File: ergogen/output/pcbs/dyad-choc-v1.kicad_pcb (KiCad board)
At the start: 2 copper layers, 117.6 x 96.6 mm, 84 parts

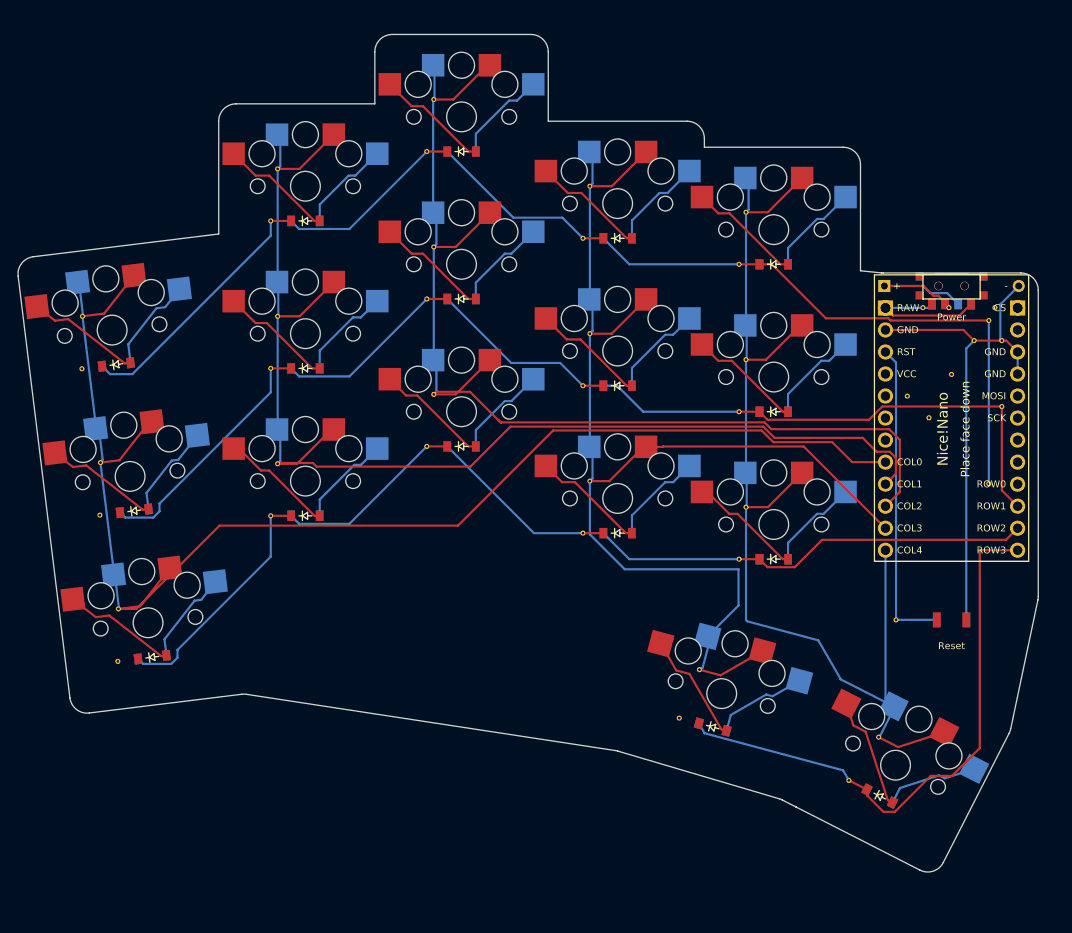
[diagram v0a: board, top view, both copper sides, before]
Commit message: Rename and adding reverse side labels
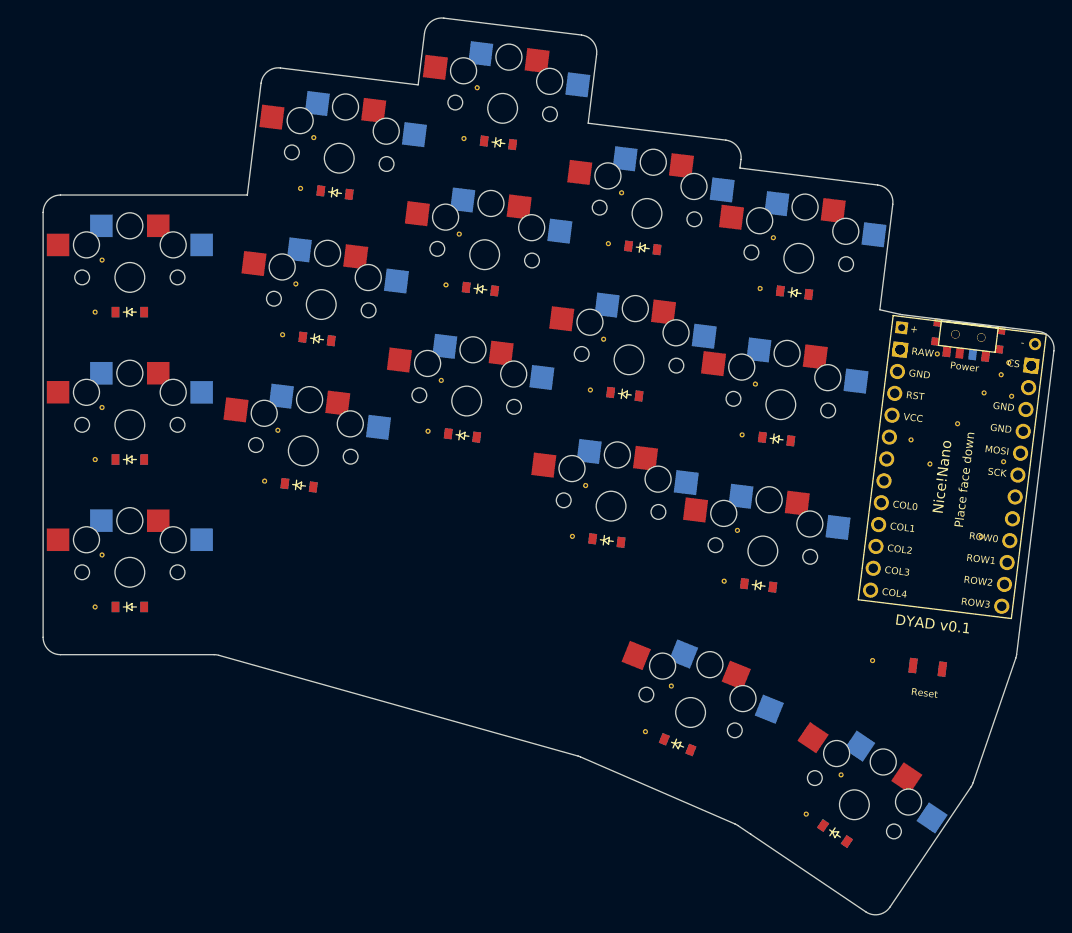
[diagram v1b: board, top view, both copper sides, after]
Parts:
- removed the REF** at (257.3, 133.3)
- removed the REF** at (156.5, 153.4)
- removed the REF** at (231.0, 135.5)
- removed the REF** at (259.0, 149.8)
- removed the REF** at (230.2, 124.5)
- removed the REF** at (177.0, 130.5)
- removed the REF** at (158.6, 170.3)
- removed the REF** at (176.2, 119.5)
- removed the REF** at (251.4, 129.5)
- removed the REF** at (213.0, 132.5)
- removed the REF** at (194.2, 145.5)
- removed the REF** at (225.7, 171.2)
- removed the REF** at (194.2, 111.5)
- removed the REF** at (176.2, 136.5)
- removed the REF** at (231.0, 152.5)
- removed the REF** at (195.0, 139.5)
- removed the REF** at (231.0, 118.5)
- removed the REF** at (212.2, 155.5)
- removed the REF** at (254.7, 137.2)
- removed the REF** at (254.4, 129.5)
- removed the REF** at (177.0, 113.5)
- removed the REF** at (223.3, 176.8)
- removed the REF** at (248.3, 165.5)
- removed the REF** at (176.2, 153.5)
- removed the REF** at (154.5, 136.5)
- removed the REF** at (246.3, 179.0)
- removed the REF** at (212.2, 121.5)
- removed the REF** at (154.5, 130.5)
- removed the REF** at (213.0, 149.5)
- removed the REF** at (252.1, 142.2)
- removed the REF** at (195.0, 105.5)
- removed the REF** at (260.5, 140.9)
- removed the REF** at (230.2, 141.5)
- removed the REF** at (259.7, 129.5)
- removed the REF** at (194.2, 128.5)
- removed the REF** at (158.7, 164.2)
- removed the REF** at (195.0, 122.5)
- removed the REF** at (260.5, 133.3)
- removed the REF** at (230.2, 158.5)
- removed the REF** at (249.6, 139.7)
- removed the REF** at (213.0, 115.5)
- removed the REF** at (242.9, 184.0)
- removed the REF** at (156.6, 147.4)
- removed the REF** at (259.0, 131.0)
- removed the REF** at (177.0, 147.5)
- removed the REF** at (212.2, 138.5)
- added REF**: VIA-0.6mm, VIA-0.6mm, F.Cu at (156.0, 164.0)
- added REF**: VIA-0.6mm, VIA-0.6mm, F.Cu at (211.0, 155.9)
- added REF**: VIA-0.6mm, VIA-0.6mm, F.Cu at (213.1, 139.0)
- added REF**: VIA-0.6mm, VIA-0.6mm, F.Cu at (215.2, 122.1)
- added REF**: VIA-0.6mm, VIA-0.6mm, F.Cu at (228.5, 161.0)
- added REF**: VIA-0.6mm, VIA-0.6mm, F.Cu at (230.6, 144.2)
- added REF**: VIA-0.6mm, VIA-0.6mm, F.Cu at (232.7, 127.3)
- added REF**: VIA-0.6mm, VIA-0.6mm, F.Cu at (219.4, 178.4)
- added REF**: VIA-0.6mm, VIA-0.6mm, F.Cu at (238.0, 187.9)
- added REF**: VIA-0.6mm, VIA-0.6mm, F.Cu at (156.8, 158.0)
- added REF**: VIA-0.6mm, VIA-0.6mm, F.Cu at (156.8, 141.0)
- added REF**: VIA-0.6mm, VIA-0.6mm, F.Cu at (156.0, 147.0)
- added REF**: VIA-0.6mm, VIA-0.6mm, F.Cu at (156.8, 124.0)
- added REF**: VIA-0.6mm, VIA-0.6mm, F.Cu at (177.1, 143.6)
- added REF**: VIA-0.6mm, VIA-0.6mm, F.Cu at (179.1, 126.8)
- added REF**: VIA-0.6mm, VIA-0.6mm, F.Cu at (181.2, 109.9)
- added REF**: VIA-0.6mm, VIA-0.6mm, F.Cu at (195.9, 137.9)
- added REF**: VIA-0.6mm, VIA-0.6mm, F.Cu at (198.0, 121.0)
- added REF**: VIA-0.6mm, VIA-0.6mm, F.Cu at (200.1, 104.1)
- added REF**: VIA-0.6mm, VIA-0.6mm, F.Cu at (212.6, 150.0)
- added REF**: VIA-0.6mm, VIA-0.6mm, F.Cu at (214.6, 133.1)
- added REF**: VIA-0.6mm, VIA-0.6mm, F.Cu at (216.7, 116.3)
- added REF**: VIA-0.6mm, VIA-0.6mm, F.Cu at (156.0, 130.0)
- added REF**: VIA-0.6mm, VIA-0.6mm, F.Cu at (230.1, 155.2)
- added REF**: VIA-0.6mm, VIA-0.6mm, F.Cu at (232.1, 138.3)
- added REF**: VIA-0.6mm, VIA-0.6mm, F.Cu at (234.2, 121.4)
- added REF**: VIA-0.6mm, VIA-0.6mm, F.Cu at (222.4, 173.1)
- added REF**: VIA-0.6mm, VIA-0.6mm, F.Cu at (242.0, 183.4)
- added REF**: VIA-0.6mm, VIA-0.6mm, F.Cu at (261.7, 139.7)
- added REF**: VIA-0.6mm, VIA-0.6mm, F.Cu at (258.5, 139.3)
- added REF**: VIA-0.6mm, VIA-0.6mm, F.Cu at (260.5, 137.2)
- added REF**: VIA-0.6mm, VIA-0.6mm, F.Cu at (258.2, 155.9)
- added REF**: VIA-0.6mm, VIA-0.6mm, F.Cu at (261.3, 135.8)
- added REF**: VIA-0.6mm, VIA-0.6mm, F.Cu at (175.5, 149.5)
- added REF**: VIA-0.6mm, VIA-0.6mm, F.Cu at (250.1, 144.7)
- added REF**: VIA-0.6mm, VIA-0.6mm, F.Cu at (252.3, 147.5)
- added REF**: VIA-0.6mm, VIA-0.6mm, F.Cu at (253.1, 134.8)
- added REF**: VIA-0.6mm, VIA-0.6mm, F.Cu at (255.4, 142.9)
- added REF**: VIA-0.6mm, VIA-0.6mm, F.Cu at (260.7, 147.3)
- added REF**: VIA-0.6mm, VIA-0.6mm, F.Cu at (245.6, 170.2)
- added REF**: VIA-0.6mm, VIA-0.6mm, F.Cu at (177.6, 132.6)
- added REF**: VIA-0.6mm, VIA-0.6mm, F.Cu at (179.7, 115.7)
- added REF**: VIA-0.6mm, VIA-0.6mm, F.Cu at (194.4, 143.7)
- added REF**: VIA-0.6mm, VIA-0.6mm, F.Cu at (196.5, 126.9)
- added REF**: VIA-0.6mm, VIA-0.6mm, F.Cu at (198.5, 110.0)
- moved D17 6.73 mm to (241.3, 190.1), turned to -34 degrees
- moved S17 6.58 mm to (243.5, 186.8), turned to -34 degrees
- moved S3 6.41 mm to (160.0, 126.0), turned to 0 degrees
- moved D1 6.34 mm to (160.0, 164.0), turned to 0 degrees
- moved D3 6.24 mm to (160.0, 130.0), turned to 0 degrees
- moved S1 6.19 mm to (160.0, 160.0), turned to 0 degrees
- moved ? 6.13 mm to (252.0, 171.0), turned to 173 degrees
- moved ? 6.08 mm to (256.7, 132.7), turned to -97 degrees
- moved T1 6.08 mm to (256.7, 132.7), turned to -7 degrees
- moved S2 5.95 mm to (160.0, 143.0), turned to 0 degrees
- moved D2 5.94 mm to (160.0, 147.0), turned to 0 degrees
- moved MCU1 5.64 mm to (254.7, 149.1), turned to -97 degrees
- moved S6 5.06 mm to (184.1, 112.3), turned to -7 degrees
- moved S9 4.84 mm to (203.0, 106.5), turned to -7 degrees
- moved D6 4.72 mm to (183.7, 116.2), turned to -7 degrees
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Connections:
- MCU1 pad : RAW -> CS
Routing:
- net COL0: track 161.3 -> 0.00 mm
- net ROW0: track 141.9 -> 0.00 mm
- net COL1: track 141.4 -> 0.00 mm
- net COL3: track 141.2 -> 0.00 mm
- net ROW1: track 133.9 -> 0.00 mm
- net COL2: track 128.0 -> 0.00 mm
- net COL4: track 127.1 -> 0.00 mm
- net ROW2: track 123.7 -> 0.00 mm
- net ROW3: track 66.2 -> 0.00 mm
- net GND: track 58.7 -> 0.00 mm
- net RST: track 36.1 -> 0.00 mm
- net pinky_top: track 24.2 -> 0.00 mm
- net ring_home: track 24.2 -> 0.00 mm
- net middle_top: track 24.2 -> 0.00 mm
- net inner_home: track 24.2 -> 0.00 mm
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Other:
- board size 117.6 x 96.6 mm -> 116.6 x 103.4 mm
- net class Default added: clearance 0.2, trace_width 0.25, via_dia 0.8, via_drill 0.4
